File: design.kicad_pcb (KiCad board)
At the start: 2 copper layers, 80 x 55 mm, 88 parts, among them J1 2601-3108, J10 Conn_01x04, J11 Conn_01x04, J12 Conn_01x03, J13 Conn_01x03, J14 BM04B-SRSS-TB_LF__SN_, J2 2601-3108, J3 2601-3108, J4 TYPE-C-31-M-12, J5 SKEDD-UPDI-4, J6 Conn_01x04, J7 Conn_01x04, J8 Conn_01x04, J9 Conn_01x04, U1 ATtiny1616-S, U2 AP2112K-3.3, U3 CP2105, U4 ATtiny1616-M

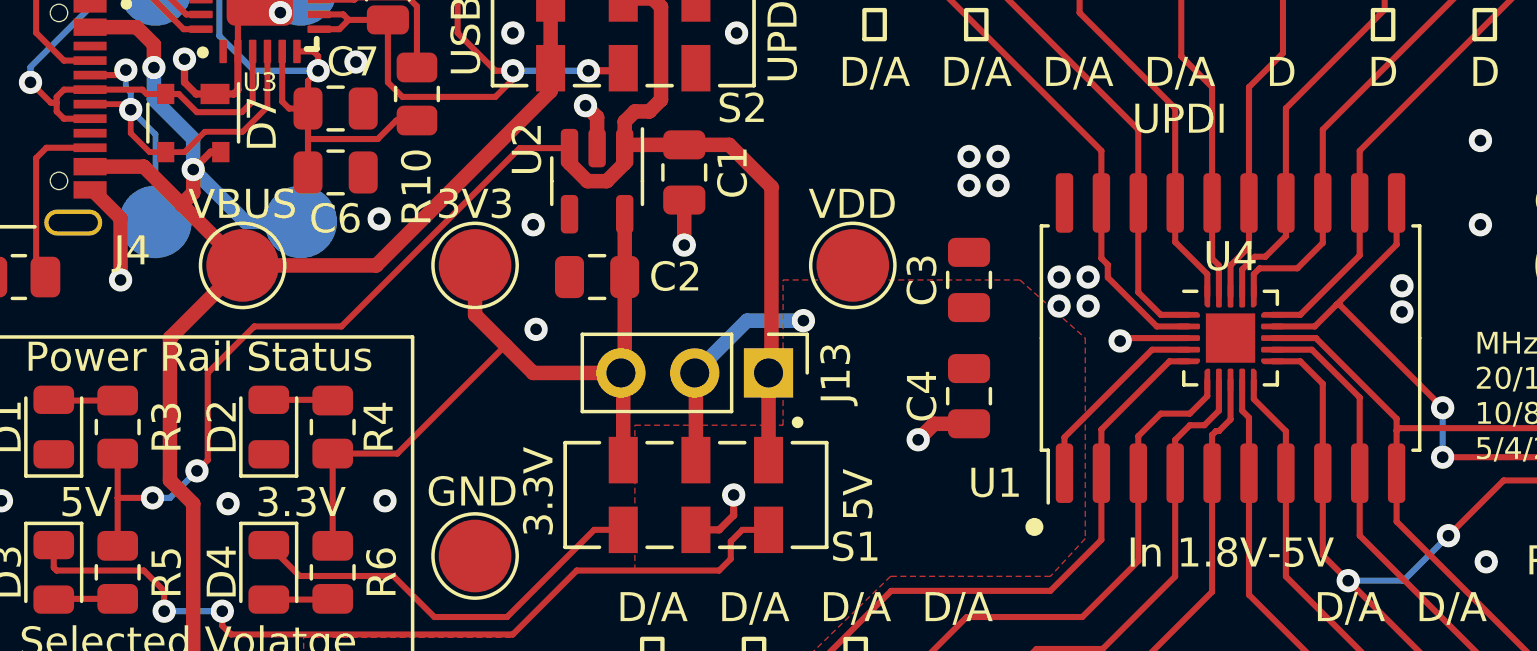
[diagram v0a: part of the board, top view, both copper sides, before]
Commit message: small minor updates
DRC issues
make traces lean
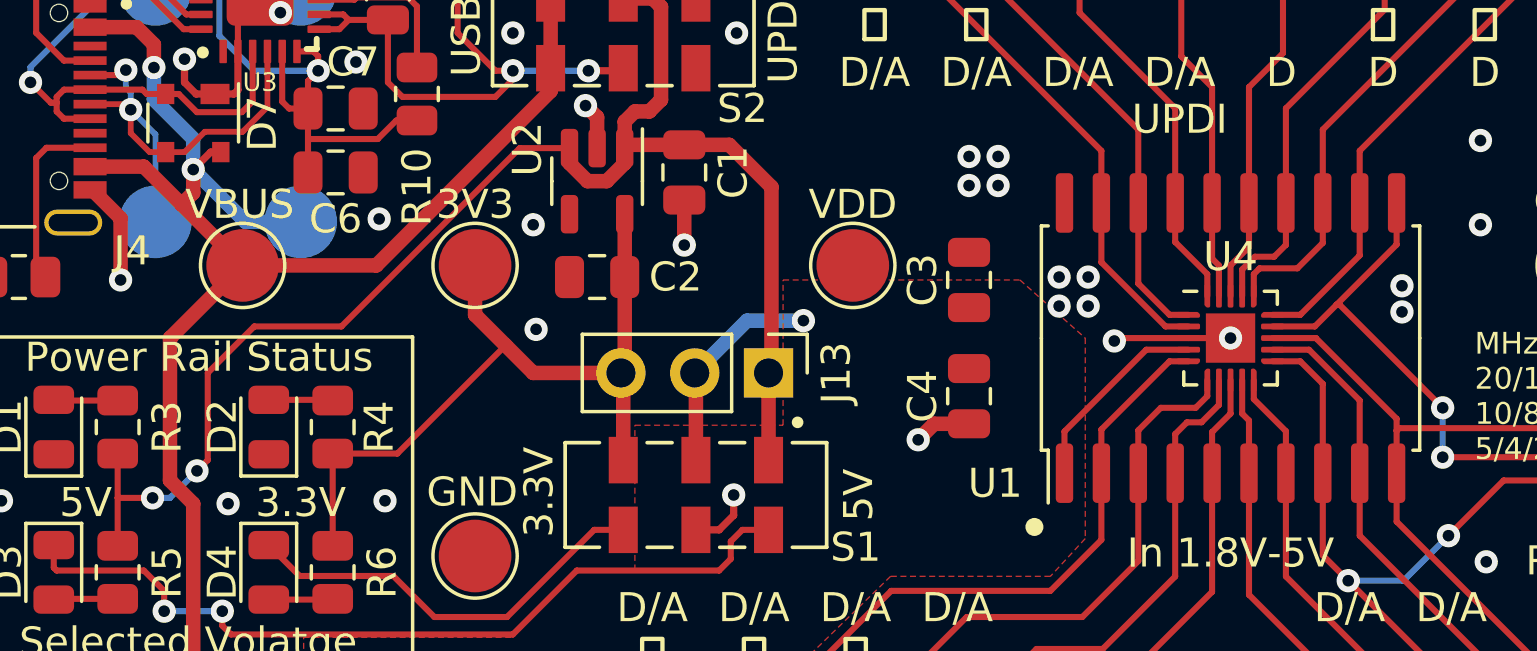
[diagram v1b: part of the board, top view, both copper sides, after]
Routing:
- net GND: track 42.0 -> 43.6 mm, vias 68 -> 69

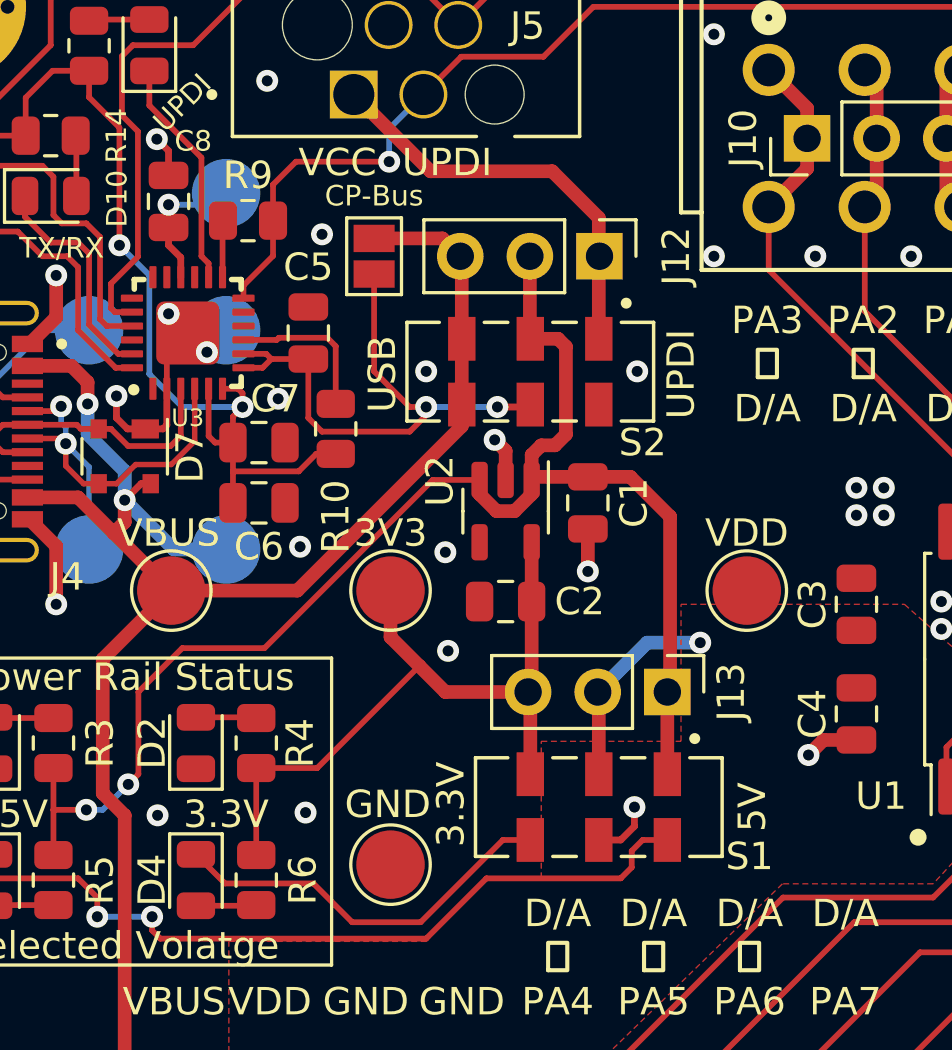
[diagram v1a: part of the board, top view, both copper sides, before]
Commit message: change to K3-2235S-K1 / JS202011SCQN DPDT Switch
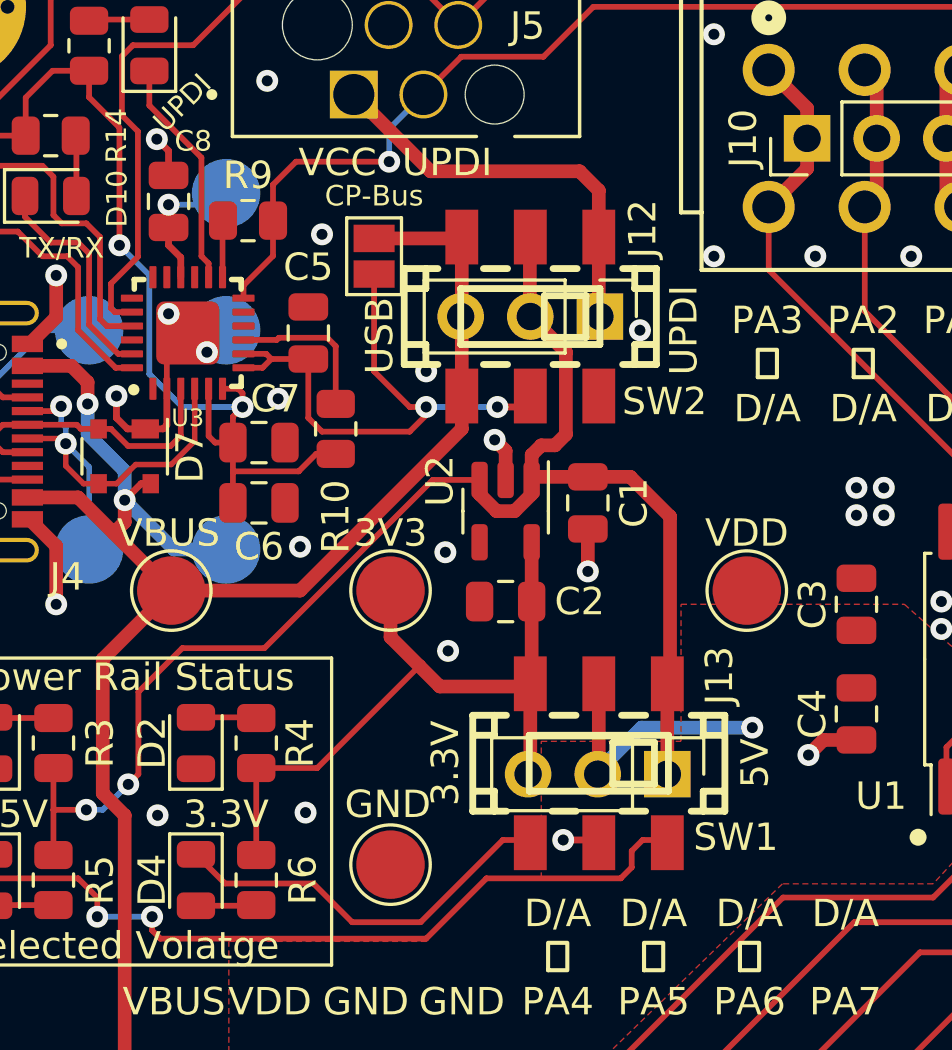
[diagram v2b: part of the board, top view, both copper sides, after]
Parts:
- removed S1, S2: JS202011JCQN, Snapeda:SW_JS202011JCQN
- added SW1: K3-2235S-K1, Snapeda:easyeda2kicad_SW-SMD_K3-2235S-K1, F.Cu at (114.6, 96.8)
- added SW2: K3-2235S-K1, Snapeda:easyeda2kicad_SW-SMD_K3-2235S-K1, F.Cu at (112.1, 80.5)
- C1, C2, C5, C6: value 1uF -> 1uF 50V X7R ±10%
- C3, C7: value 0.1uF -> 100nF 50V X7R ±10%
- C4: value 10uF -> 10uF 25V X5R ±10%
- C8: value 4,7uF -> 4.7uF 25V X5R ±10%
- moved J13 3.00 mm to (117.1, 97.2)
- moved J12 2.20 mm to (114.6, 80.5)
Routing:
- net VDD: track 44.1 -> 45.9 mm
- net GND: track 43.6 -> 42.7 mm
- net V_switch: track 54.1 -> 53.5 mm

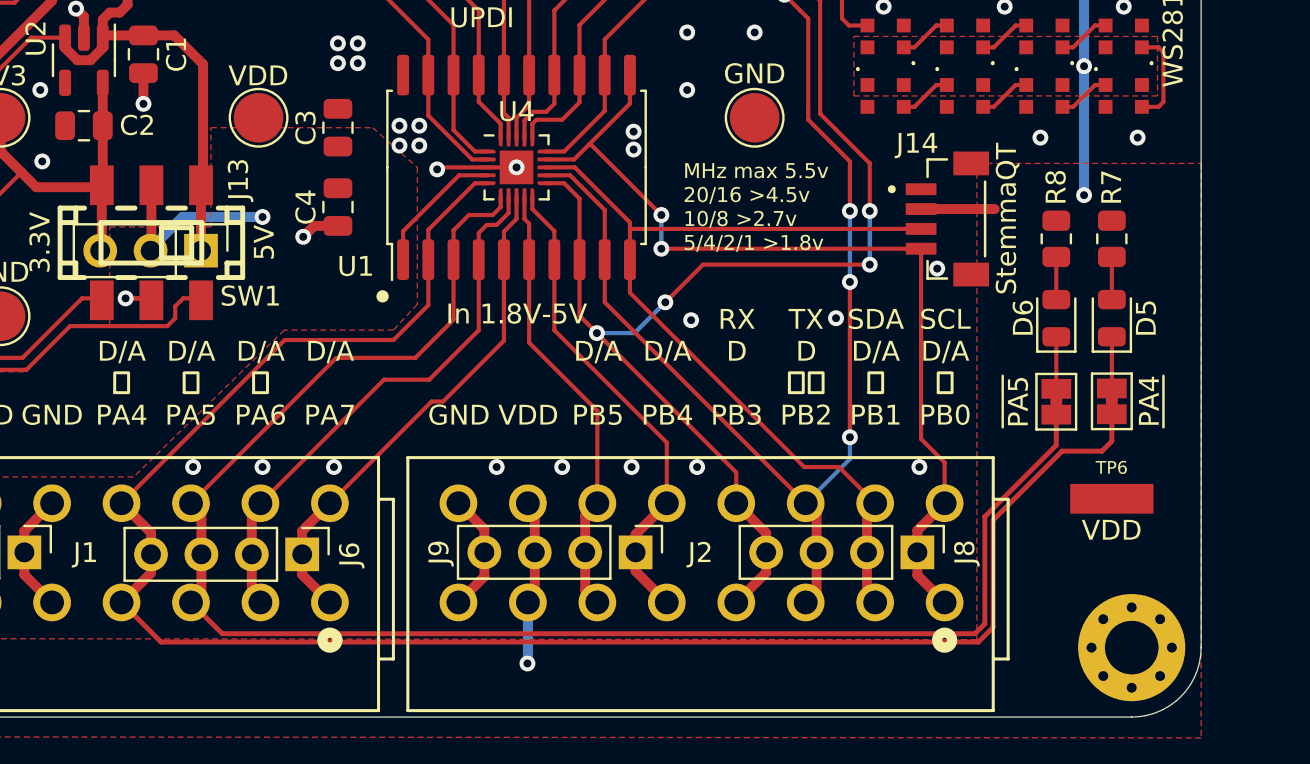
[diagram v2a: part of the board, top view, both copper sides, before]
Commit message: Add MOSFET for GPIO LEDs
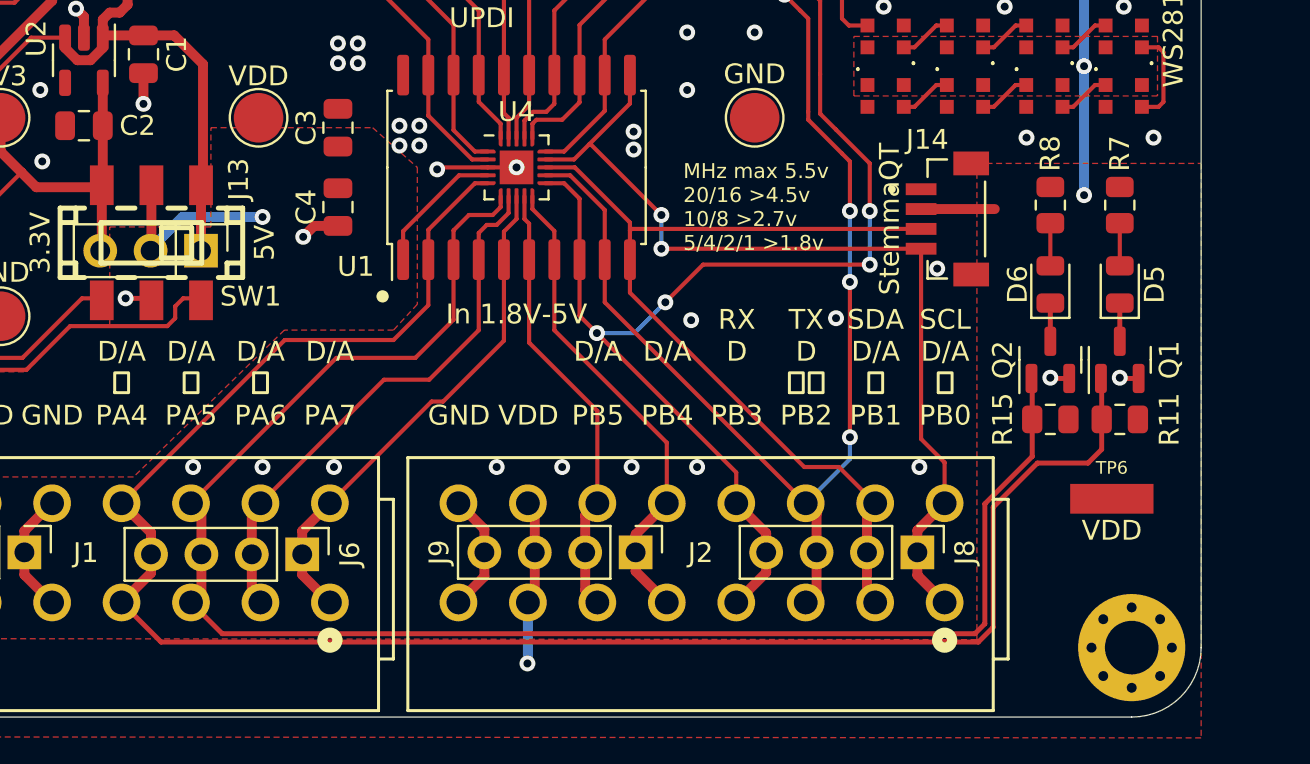
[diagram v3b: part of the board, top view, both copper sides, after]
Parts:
- removed JP2: PA4, Jumper:SolderJumper-2_P1.3mm_Bridged_Pad1.0x1.5mm
- removed JP3: PA5, Jumper:SolderJumper-2_P1.3mm_Bridged_Pad1.0x1.5mm
- added Q1: AO3400A, Package_TO_SOT_SMD:SOT-23, F.Cu at (163.4, 102.7)
- added Q2: AO3400A, Package_TO_SOT_SMD:SOT-23, F.Cu at (159.9, 102.7)
- added R11: 4.7k, Resistor_SMD:R_0805_2012Metric, F.Cu at (163.4, 105.7)
- added R15: 4.7k, Resistor_SMD:R_0805_2012Metric, F.Cu at (159.9, 105.7)
- moved D5 1.75 mm to (163.4, 98.9)
- moved R7 1.75 mm to (163.4, 94.9)
- moved D6 1.73 mm to (159.9, 98.9)
- moved R8 1.73 mm to (159.9, 94.9)
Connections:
- D5 pad 1: LED1 -> Net-(D5-Pad1)
- D6 pad 1: LED2 -> Net-(D6-Pad1)
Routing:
- net LED2: track 2.62 -> 0.00 mm
- net LED1: track 2.60 -> 0.00 mm
- net GND: track 42.7 -> 44.6 mm, vias 69 -> 71
- net Net-(D6-Pad1): track 0.00 -> 1.92 mm
- net Net-(D5-Pad1): track 0.00 -> 1.92 mm
- net PA4: track 93.0 -> 95.0 mm
- net PA5: track 83.3 -> 84.6 mm

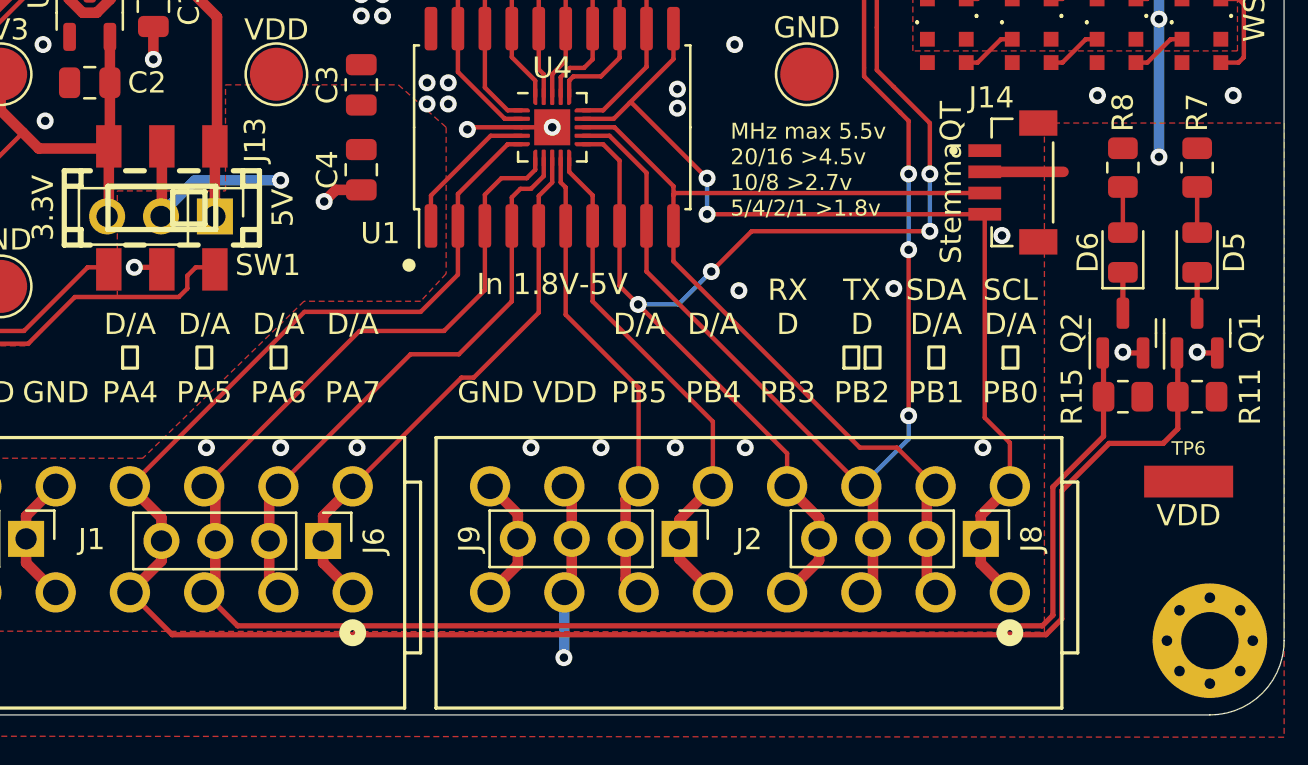
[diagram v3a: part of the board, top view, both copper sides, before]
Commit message: Add Gate Resistor MOSFET
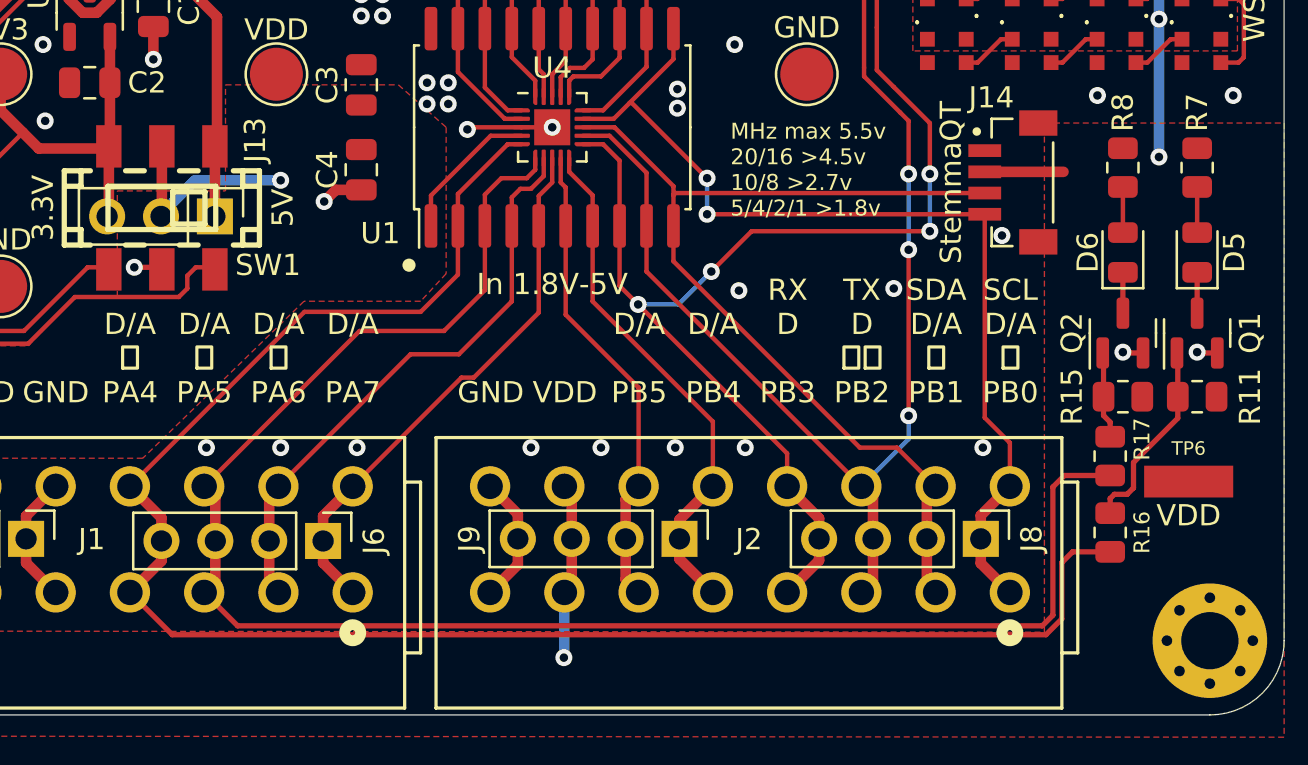
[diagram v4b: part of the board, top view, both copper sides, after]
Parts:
- added R16: 220, Resistor_SMD:R_0805_2012Metric, F.Cu at (159.3, 112.1)
- added R17: 220, Resistor_SMD:R_0805_2012Metric, F.Cu at (159.3, 108.5)
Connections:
- Q1 pad 1: PA4 -> Net-(Q1-Pad1)
- Q2 pad 1: PA5 -> Net-(Q2-Pad1)
- R11 pad 1: PA4 -> Net-(Q1-Pad1)
- R15 pad 1: PA5 -> Net-(Q2-Pad1)
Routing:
- net PA4: track 95.0 -> 83.8 mm
- net Net-(Q1-Pad1): track 0.00 -> 9.24 mm
- net PA5: track 84.6 -> 80.2 mm
- net Net-(Q2-Pad1): track 0.00 -> 4.09 mm

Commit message: Update design.kicad_pcb
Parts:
- U4: footprint Package_DFN_QFN:VQFN-20-1EP_3x3mm_P0.4mm_EP1.7x1.7mm -> Snapeda:ATTINY1616-MFR_QFN40P300X300X90-21N

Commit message: Update design.kicad_pcb
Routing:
- net GND: vias 71 -> 72
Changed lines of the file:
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@@
     (property "Sheetname" "")
     (attr smd)
-    (fp_text reference "U4" (at 0.865 -3.74) (layer "F.SilkS")
+    (fp_text reference "U4" (at 3 -1.5) (layer "F.SilkS")
       (effects (font (size 1 1) (thickness 0.15)))
     )
@@
     (property "Sheetname" "")
     (attr smd)
-    (fp_text reference "U1" (at -5 -8.1 180) (layer "F.SilkS")
+    (fp_text reference "U1" (at -5 -7.7 180) (layer "F.SilkS")
       (effects (font (size 1 1) (thickness 0.15)))
     )
@@
   (via (at 116.1 81) (size 0.8) (drill 0.4) (layers "F.Cu" "B.Cu") (free) (net 28))
   (via (at 128.1 91.9) (size 0.8) (drill 0.4) (layers "F.Cu" "B.Cu") (free) (net 28))
+  (via (at 155.3 94.2) (size 0.8) (drill 0.4) (layers "F.Cu" "B.Cu") (free) (net 28))
   (via (at 129.6 78.3) (size 0.8) (drill 0.4) (layers "F.Cu" "B.Cu") (free) (net 28))
   (via (at 158.7 91.5) (size 0.8) (drill 0.4) (layers "F.Cu" "B.Cu") (free) (net 28))
